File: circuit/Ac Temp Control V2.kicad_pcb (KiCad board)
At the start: 2 copper layers, 74.9 x 69.8 mm, 20 parts, among them J1 Conn_01x02_Male, J2 Conn_01x05_Male, Q1 P2N2222A, SW1 SW_Push, U1 ATmega328-P, U2 DHT11, U3 TSOP382xx, U4 CAT24C256, Y1 16MHZ

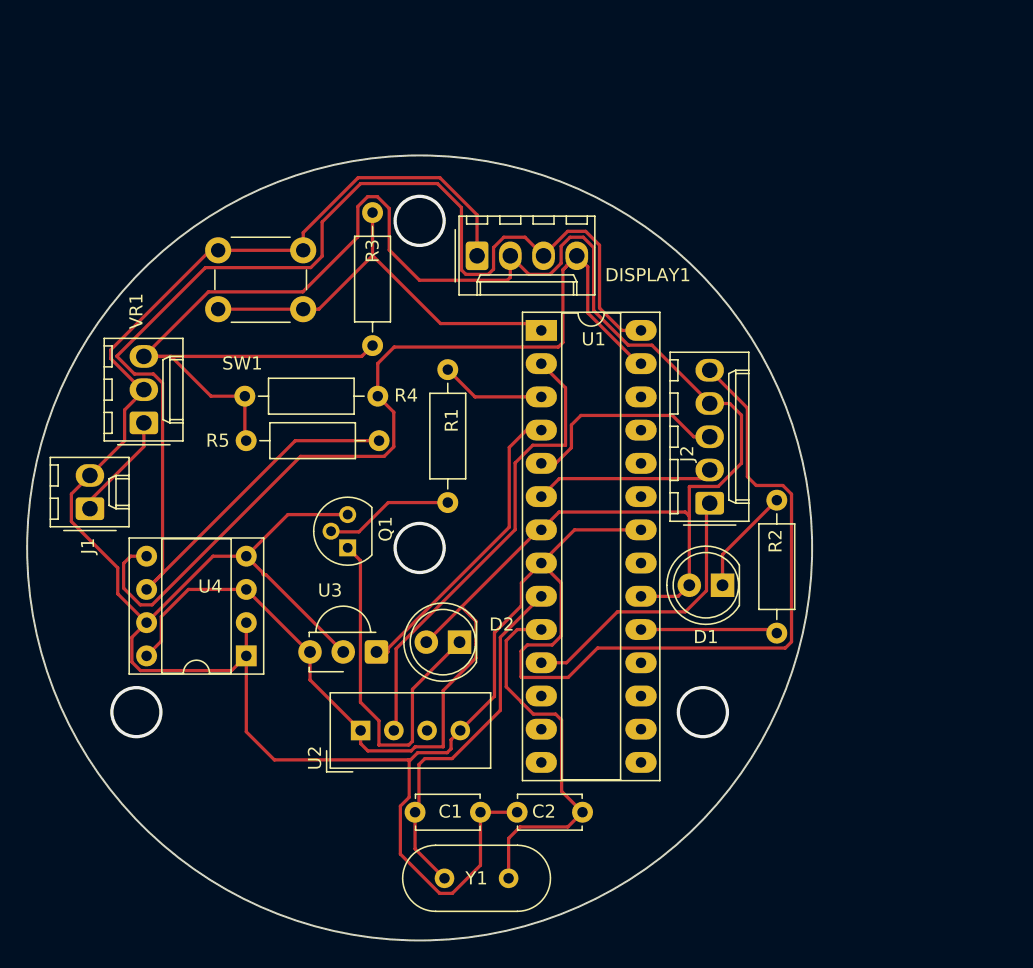
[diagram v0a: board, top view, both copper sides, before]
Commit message: Version 2 with 0.6mm track width and clearance made. gerber file generated
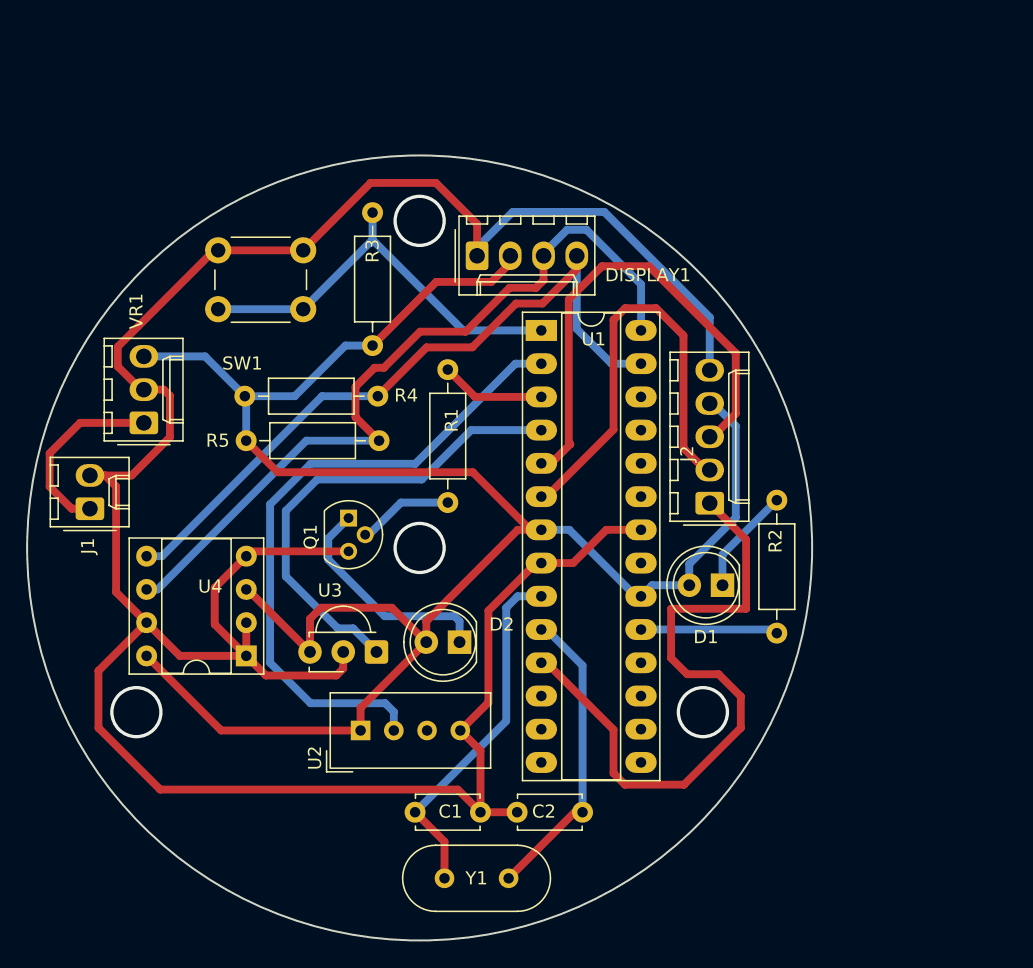
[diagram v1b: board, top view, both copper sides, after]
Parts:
- moved Q1 2.27 mm to (139.1, 102.2), turned to -90 degrees
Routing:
- net Net-(DISPLAY1-Pad3): track 105.3 -> 60.8 mm
- net Net-(D1-Pad2): track 189.5 -> 153.5 mm
- net GND: track 239.7 -> 208.6 mm
- net Net-(J2-Pad1): track 21.7 -> 50.5 mm
- net Net-(J2-Pad3): track 16.6 -> 37.8 mm
- net Net-(J2-Pad2): track 13.7 -> 33.9 mm
- net Net-(DISPLAY1-Pad4): track 70.7 -> 54.6 mm
- net Net-(U1-Pad2): track 35.7 -> 49.7 mm
- net Net-(U1-Pad4): track 23.4 -> 36.4 mm
- net Net-(D2-PadA): track 27.8 -> 17.4 mm
- net Net-(J1-Pad1): track 8.27 -> 14.5 mm
- net Net-(C2-Pad1): track 29.1 -> 23.2 mm
- net Net-(Q1-Pad2): track 9.87 -> 7.05 mm
- net Net-(D1-Pad1): track 8.92 -> 8.22 mm
